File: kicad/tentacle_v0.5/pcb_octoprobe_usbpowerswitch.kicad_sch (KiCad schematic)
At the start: 4 parts, among them U1401 MT9700

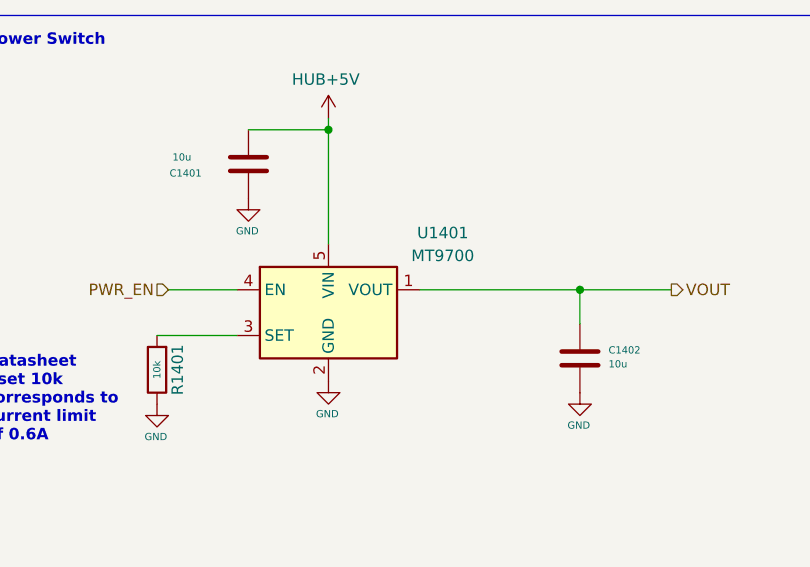
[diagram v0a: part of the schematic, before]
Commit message: Schematics: Fix ERC warnings
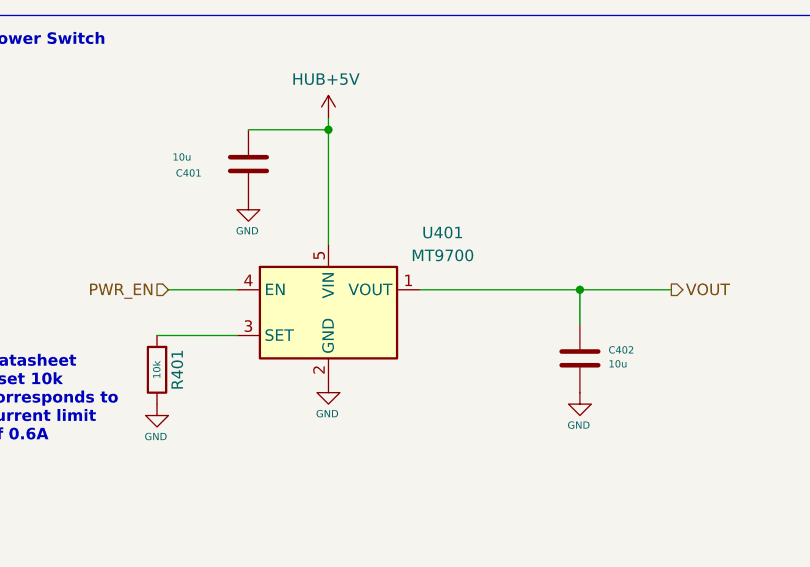
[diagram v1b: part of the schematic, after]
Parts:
- renumbered C1401 to C401, C1402 to C402, R1401 to R401, U1401 to U401
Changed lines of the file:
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@@
 (kicad_sch
-	(version 20231120)
+	(version 20250114)
 	(generator "eeschema")
-	(generator_version "8.0")
+	(generator_version "9.0")
 	(paper "A4")
 	(title_block
@@
 		(comment 1 "The MIT License (MIT)")
 	)
-	(junction
-		(at 127 81.28)
-		(diameter 0)
-		(color 0 0 0 0)
-	)
-	(junction
-		(at 99.06 63.5)
-		(diameter 0)
-		(color 0 0 0 0)
-	)
-	(wire
-		(pts
-			(xy 127 85.09) (xy 127 81.28)
-		)
-		(stroke
-			(width 0)
-			(type default)
-		)
-	)
-	(wire
-		(pts
-			(xy 81.28 81.28) (xy 88.9 81.28)
-		)
-		(stroke
-			(width 0)
-			(type default)
-		)
-	)
-	(wire
-		(pts
-			(xy 99.06 62.23) (xy 99.06 63.5)
-		)
-		(stroke
-			(width 0)
-			(type default)
-		)
-	)
-	(wire
-		(pts
-			(xy 90.17 63.5) (xy 99.06 63.5)
-		)
-		(stroke
-			(width 0)
-			(type default)
-		)
-	)
-	(wire
-		(pts
-			(xy 127 81.28) (xy 137.16 81.28)
-		)
-		(stroke
-			(width 0)
-			(type default)
-		)
-	)
-	(wire
-		(pts
-			(xy 80.01 86.36) (xy 88.9 86.36)
-		)
-		(stroke
-			(width 0)
-			(type default)
-		)
-	)
-	(wire
-		(pts
-			(xy 109.22 81.28) (xy 127 81.28)
-		)
-		(stroke
-			(width 0)
-			(type default)
-		)
-	)
-	(wire
-		(pts
-			(xy 99.06 63.5) (xy 99.06 76.2)
-		)
-		(stroke
-			(width 0)
-			(type default)
-		)
-	)
 	(rectangle
 		(start 54.61 50.8)
@@
 		)
 	)
+	(junction
+		(at 127 81.28)
+		(diameter 0)
+		(color 0 0 0 0)
+	)
+	(junction
+		(at 99.06 63.5)
+		(diameter 0)
+		(color 0 0 0 0)
+	)
+	(wire
+		(pts
+			(xy 127 85.09) (xy 127 81.28)
+		)
+		(stroke
+			(width 0)
+			(type default)
+		)
+	)
+	(wire
+		(pts
+			(xy 81.28 81.28) (xy 88.9 81.28)
+		)
+		(stroke
+			(width 0)
+			(type default)
+		)
+	)
+	(wire
+		(pts
+			(xy 99.06 62.23) (xy 99.06 63.5)
+		)
+		(stroke
+			(width 0)
+			(type default)
+		)
+	)
+	(wire
+		(pts
+			(xy 90.17 63.5) (xy 99.06 63.5)
+		)
+		(stroke
+			(width 0)
+			(type default)
+		)
+	)
+	(wire
+		(pts
+			(xy 127 81.28) (xy 137.16 81.28)
+		)
+		(stroke
+			(width 0)
+			(type default)
+		)
+	)
+	(wire
+		(pts
+			(xy 80.01 86.36) (xy 88.9 86.36)
+		)
+		(stroke
+			(width 0)
+			(type default)
+		)
+	)
+	(wire
+		(pts
+			(xy 109.22 81.28) (xy 127 81.28)
+		)
+		(stroke
+			(width 0)
+			(type default)
+		)
+	)
+	(wire
+		(pts
+			(xy 99.06 63.5) (xy 99.06 76.2)
+		)
+		(stroke
+			(width 0)
+			(type default)
+		)
+	)
 	(hierarchical_label "PWR_EN"
 		(shape input)
@@
 		(on_board yes)
 		(dnp no)
-		(property "Reference" "C1402"
+		(property "Reference" "C402"
 			(at 130.175 87.9856 0)
 			(effects
@@
 		(on_board yes)
 		(dnp no)
-		(property "Reference" "#PWR01404"
+		(property "Reference" "#PWR0404"
 			(at 99.06 97.79 0)
 			(effects
@@
 		(dnp no)
 		(fields_autoplaced yes)
-		(property "Reference" "#SYM1401"
+		(property "Reference" "#SYM401"
 			(at 275.59 167.005 0)
 			(effects
@@
 		(on_board yes)
 		(dnp no)
-		(property "Reference" "#PWR01402"
+		(property "Reference" "#PWR0402"
 			(at 90.17 77.47 0)
 			(effects
@@
 		(on_board yes)
 		(dnp no)
-		(property "Reference" "#PWR01401"
+		(property "Reference" "#PWR0401"
 			(at 80.01 100.33 0)
 			(effects
@@
 		(on_board yes)
 		(dnp no)
-		(property "Reference" "#PWR01403"
+		(property "Reference" "#PWR0403"
 			(at 99.06 66.04 0)
 			(effects
@@
 		(dnp no)
 		(fields_autoplaced yes)
-		(property "Reference" "U1401"
+		(property "Reference" "U401"
 			(at 111.76 74.9614 0)
 			(effects
@@
 		(on_board yes)
 		(dnp no)
-		(property "Reference" "#PWR01405"
+		(property "Reference" "#PWR0405"
 			(at 127 99.06 0)
 			(effects
@@
 		(on_board yes)
 		(dnp no)
-		(property "Reference" "C1401"
+		(property "Reference" "C401"
 			(at 84.963 68.326 0)
 			(effects
@@
 		(on_board yes)
 		(dnp no)
-		(property "Reference" "R1401"
+		(property "Reference" "R401"
 			(at 82.296 90.17 90)
 			(effects
